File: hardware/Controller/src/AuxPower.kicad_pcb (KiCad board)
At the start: 2 copper layers, 90 x 90 mm, 123 parts, among them J1 MC 1,5/2, J10 MC 1,5/4, J11 S3B-XH-A, J12 S3B-XH-A, J13 S3B-XH-A, J14 S3B-XH-A, J15 S3B-XH-A, J16 B3B-XH-A, J17 B4B-XH-A, J2 MC 1,5/2, J3 MC 1,5/2, J4 MC 1,5/2, J5 MC 1,5/2, J6 MC 1,5/4, J7 MC 1,5/4, J8 MC 1,5/4, J9 MC 1,5/4, Q1 BC846B,235, Q10 AO4421, Q2 BC846B,235, Q3 BC846B,235, Q4 BC846B,235, Q5 BC846B,235, Q6 AO4421, Q7 AO4421, Q8 AO4421, Q9 AO4421, U1 ZXCT1009, U2 ZXCT1009, U3 ZXCT1009, U5 ZXCT1009, U6 PIC18F26K83, U7 PI4IOE5V6416, U8 MCP9701

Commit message: Adjusted resistors a bit
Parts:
- R11: renamed from R6; value 470 -> 1K
- R12: renamed from R7; value 470 -> 1K
- R13: renamed from R8; value 470 -> 1K
- R14: renamed from R9; value 470 -> 1K
- R15: renamed from R10; value 470 -> 1K
- renumbered R15 to R10, R11 to R6, R12 to R7, R13 to R8, R14 to R9
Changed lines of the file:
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@@
 		(at 57 92 90)
 		(tags "RESC2013X70N")
-		(property "Reference" "R14"
+		(property "Reference" "R9"
 			(at 0 1.6 90)
 			(layer "B.SilkS")
@@
 		(at 25.5 92 90)
 		(tags "RESC2013X70N")
-		(property "Reference" "R11"
+		(property "Reference" "R6"
 			(at 0 1.6 90)
 			(layer "B.SilkS")
@@
 		(at 18 45 -90)
 		(tags "RESC2013X70N")
-		(property "Reference" "R6"
+		(property "Reference" "R11"
 			(at 0 1.6 90)
 			(layer "B.SilkS")
@@
 			)
 		)
-		(property "Value" "470"
+		(property "Value" "1K"
 			(at -2.3 0 0)
 			(layer "B.SilkS")
@@
 		(at 20.4 51 90)
 		(tags "RESC2013X70N")
-		(property "Reference" "R7"
+		(property "Reference" "R12"
 			(at 0 1.6 90)
 			(layer "B.SilkS")
@@
 			)
 		)
-		(property "Value" "470"
+		(property "Value" "1K"
 			(at 2.3 0 0)
 			(layer "B.SilkS")
@@
 		(at 46.5 92 90)
 		(tags "RESC2013X70N")
-		(property "Reference" "R13"
+		(property "Reference" "R8"
 			(at 0 1.6 90)
 			(layer "B.SilkS")
@@
 		(at 36 92 90)
 		(tags "RESC2013X70N")
-		(property "Reference" "R12"
+		(property "Reference" "R7"
 			(at 0 1.6 90)
 			(layer "B.SilkS")
@@
 		(at 30 51.1 90)
 		(tags "RESC2013X70N")
-		(property "Reference" "R8"
+		(property "Reference" "R13"
 			(at 0 1.6 90)
 			(layer "B.SilkS")
@@
 			)
 		)
-		(property "Value" "470"
+		(property "Value" "1K"
 			(at 2.3 0 180)
 			(layer "B.SilkS")
@@
 		(at 39.6 51 90)
 		(tags "RESC2013X70N")
-		(property "Reference" "R9"
+		(property "Reference" "R14"
 			(at 0 1.6 90)
 			(layer "B.SilkS")
@@
 			)
 		)
-		(property "Value" "470"
+		(property "Value" "1K"
 			(at 2.3 0 180)
 			(layer "B.SilkS")
@@
 		(at 49.2 51 90)
 		(tags "RESC2013X70N")
-		(property "Reference" "R10"
+		(property "Reference" "R15"
 			(at 0 1.6 90)
 			(layer "B.SilkS")
@@
 			)
 		)
-		(property "Value" "470"
+		(property "Value" "1K"
 			(at 2.3 0 180)
 			(layer "B.SilkS")
@@
 		(at 67.5 92 90)
 		(tags "RESC2013X70N")
-		(property "Reference" "R15"
+		(property "Reference" "R10"
 			(at 0 1.6 90)
 			(layer "B.SilkS")

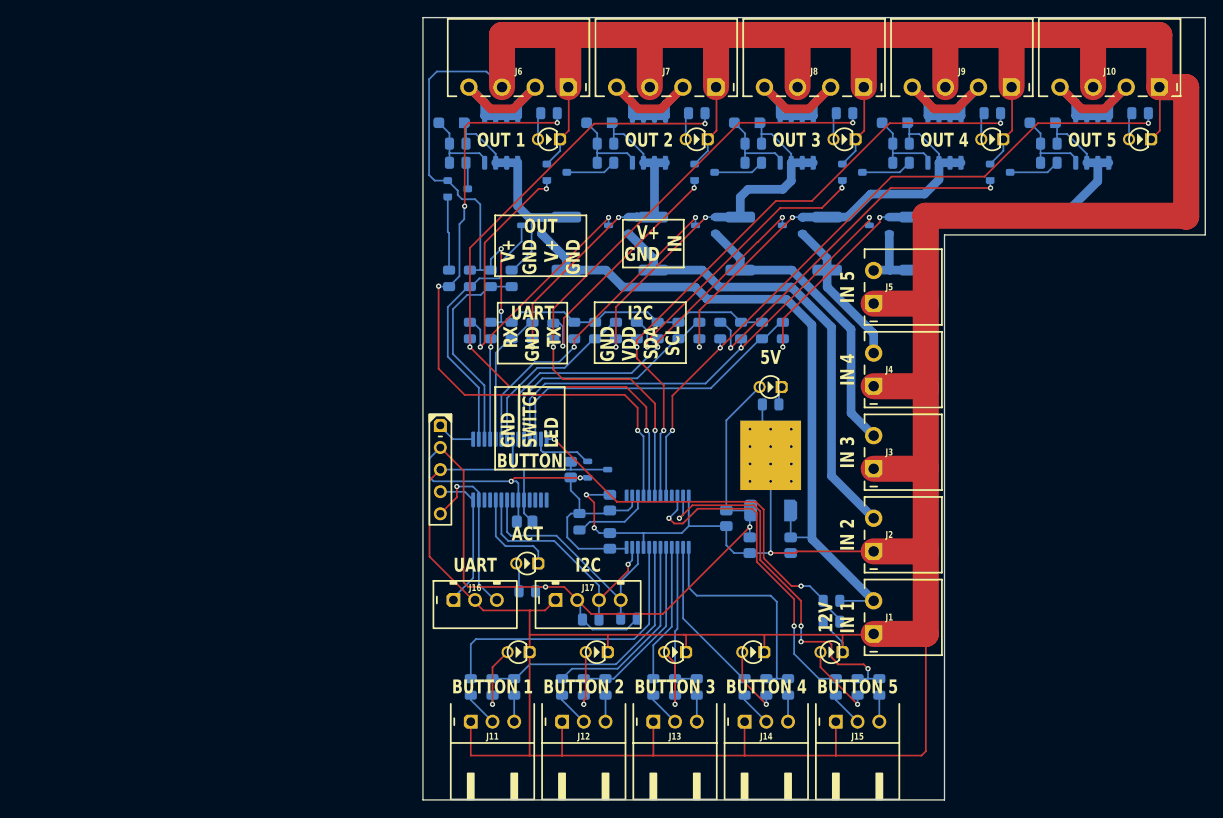
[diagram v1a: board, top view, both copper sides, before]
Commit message: Swapped PIC for SOIC variant
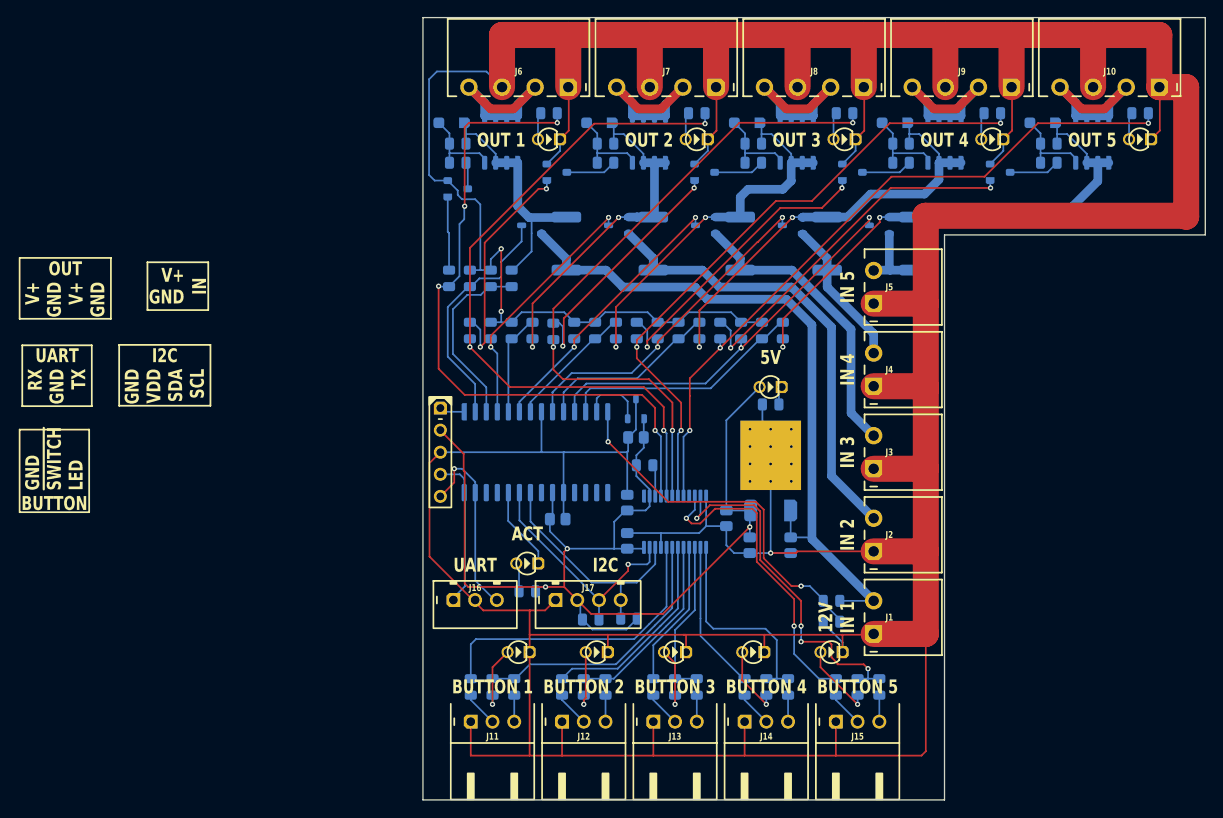
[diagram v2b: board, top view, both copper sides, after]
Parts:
- U6: footprint Medo64:U Micro [PIC18F26K83] (SSOP-28) -> Medo64:U Micro [PIC18F26K83] (SOIC-28)
- moved R33 9.92 mm to (40.5, 66.5), turned to 180 degrees
- moved C4 8.36 mm to (39.5, 63.3), turned to 180 degrees
- moved U8 8.27 mm to (39.5, 60.0), turned to 180 degrees
- moved C5 3.81 mm to (30.5, 72.7)
- moved U6 3.61 mm to (28.0, 65.0)
- moved C2 2.00 mm to (38.5, 75.2)
- moved C3 2.00 mm to (38.5, 70.8)
- moved ICSP 2.00 mm to (17.0, 65.0)
- moved U7 2.00 mm to (44.0, 73.0)
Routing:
- net 5V: track 140.1 -> 128.4 mm, vias 4 -> 3
- net ADC_VOLTAGE5: track 35.9 -> 27.5 mm
- net ADC_CURRENT5: track 54.5 -> 46.4 mm
- net ADC_VOLTAGE4: track 27.9 -> 20.5 mm
- net ADC_CURRENT4: track 46.1 -> 39.2 mm
- net ADC_VOLTAGE3: track 20.2 -> 14.1 mm
- net GND: track 692.2 -> 698.2 mm, vias 5 -> 3
- net EXPANDER_RESET: track 8.93 -> 3.27 mm
- net ADC_CURRENT3: track 38.2 -> 32.6 mm
- net ADC_VOLTAGE2: track 14.9 -> 10.7 mm
- net ADC_VOLTAGE_IN: track 45.4 -> 41.7 mm
- net ADC_CURRENT1: track 30.8 -> 27.5 mm
- net ADC_VOLTAGE1: track 24.1 -> 21.0 mm
- net ADC_CURRENT2: track 33.0 -> 30.1 mm
- net OUT_BUTTON4_LED: track 26.8 -> 24.5 mm
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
